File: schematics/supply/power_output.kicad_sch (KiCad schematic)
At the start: 41 parts, among them Q10 IRLML0030, U2 EL817, U23 TL331, U24 INA169, U9 IRS2153S

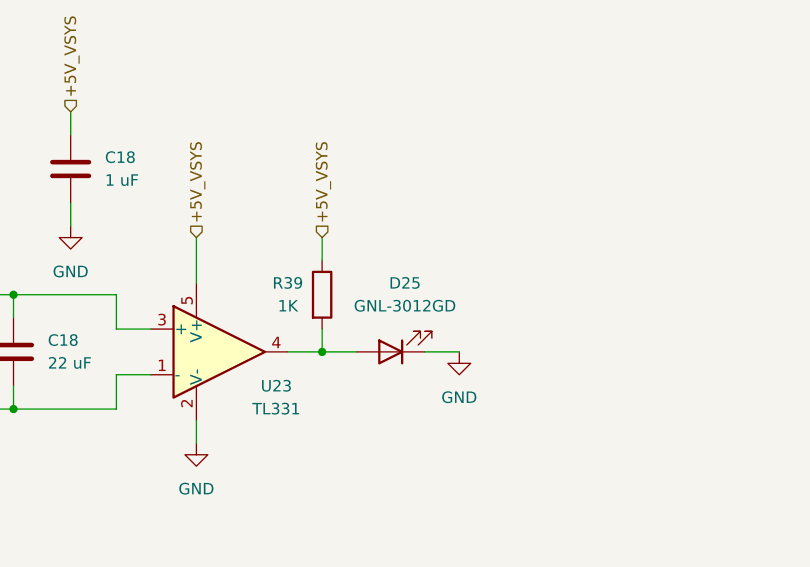
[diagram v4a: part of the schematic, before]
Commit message: Fixed problem with 20V on one leg of comparator
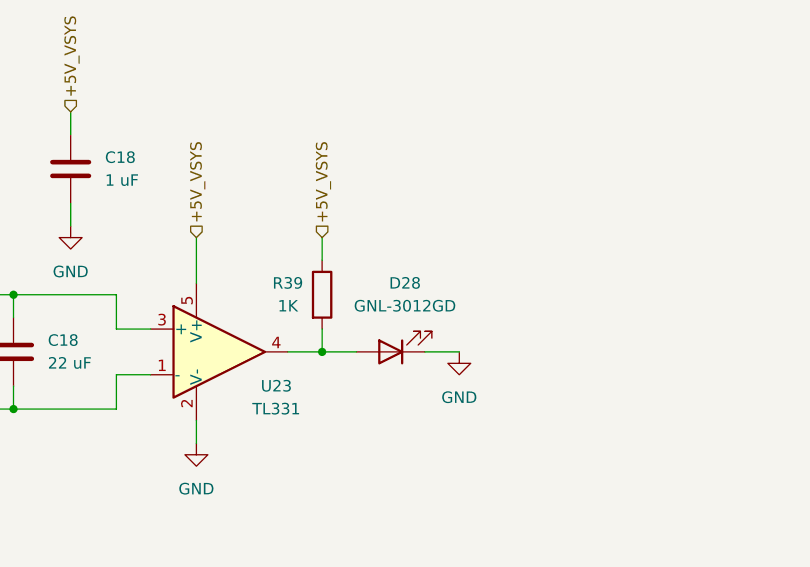
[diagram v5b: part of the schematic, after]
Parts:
- renumbered D25 to D28

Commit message: Board prepared to order
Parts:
- L2: value SPM6550T-2R2M -> SPM6550T-R68M
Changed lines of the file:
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@@
       (effects (font (size 1.27 1.27)))
     )
-    (property "Value" "SPM6550T-2R2M" (at 269.24 132.08 90)
+    (property "Value" "SPM6550T-R68M" (at 269.24 132.08 90)
       (effects (font (size 1.27 1.27)))
     )

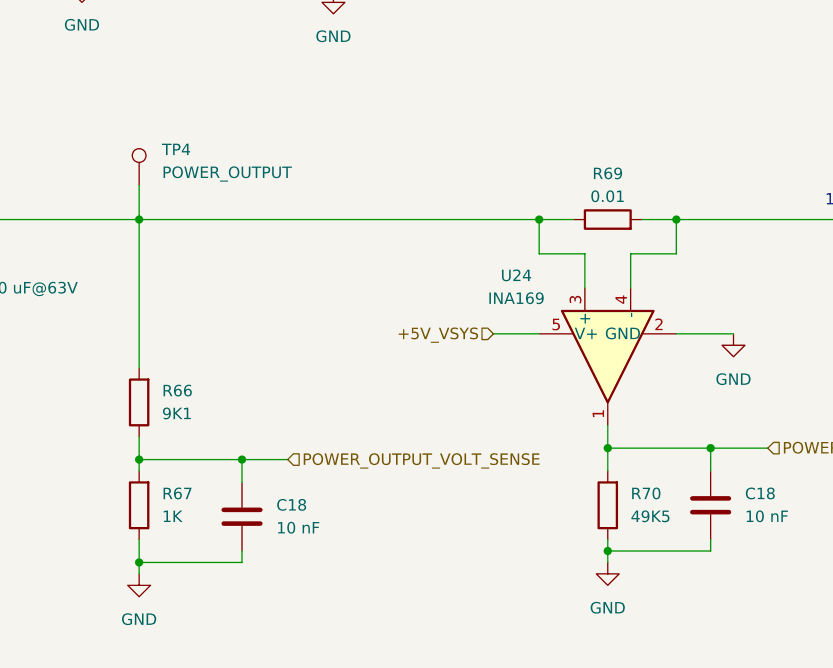
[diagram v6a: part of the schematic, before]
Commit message: One board settings changed from 4-layers to 2-layers to reduce it's price
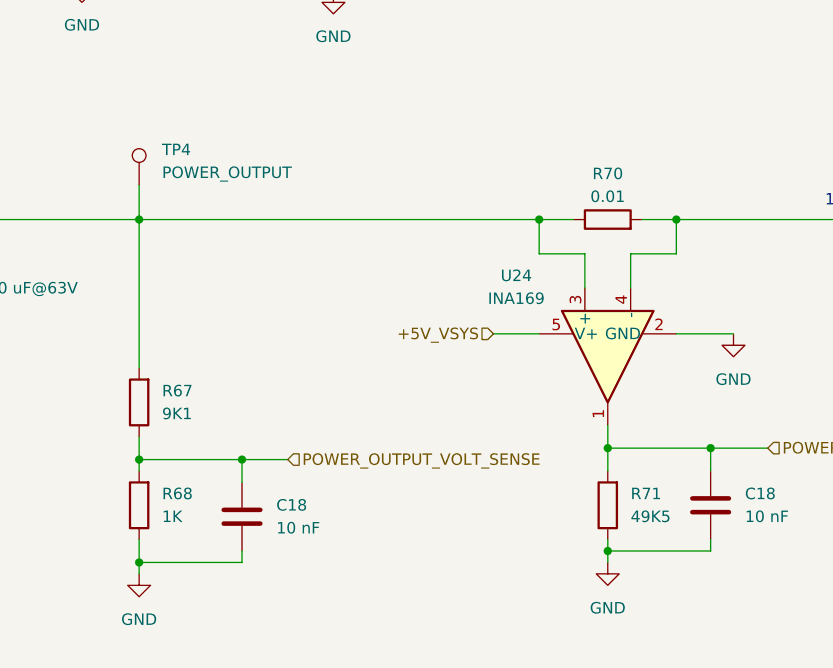
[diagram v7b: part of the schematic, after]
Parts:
- renumbered R66 to R67, R67 to R68, R69 to R70, R70 to R71
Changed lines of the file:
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@@
         )
         (path "/1e139717-fcd1-4008-a6ea-4c993845e928/4671650e-ec71-47e3-a051-fc2ad6d25f63"
-          (reference "R62") (unit 1)
+          (reference "R63") (unit 1)
         )
       )
@@
         )
         (path "/1e139717-fcd1-4008-a6ea-4c993845e928/4671650e-ec71-47e3-a051-fc2ad6d25f63"
-          (reference "R60") (unit 1)
+          (reference "R61") (unit 1)
         )
       )
@@
         )
         (path "/1e139717-fcd1-4008-a6ea-4c993845e928/4671650e-ec71-47e3-a051-fc2ad6d25f63"
-          (reference "R68") (unit 1)
+          (reference "R69") (unit 1)
         )
       )
@@
         )
         (path "/1e139717-fcd1-4008-a6ea-4c993845e928/4671650e-ec71-47e3-a051-fc2ad6d25f63"
-          (reference "R59") (unit 1)
+          (reference "R60") (unit 1)
         )
       )
@@
         )
         (path "/1e139717-fcd1-4008-a6ea-4c993845e928/4671650e-ec71-47e3-a051-fc2ad6d25f63"
-          (reference "R63") (unit 1)
+          (reference "R64") (unit 1)
         )
       )
@@
   (symbol (lib_id "Device:R") (at 358.14 167.64 180) (unit 1)
     (in_bom yes) (on_board yes) (dnp no) (fields_autoplaced)
-    (property "Reference" "R70" (at 360.68 166.37 0)
+    (property "Reference" "R71" (at 360.68 166.37 0)
       (effects (font (size 1.27 1.27)) (justify right))
     )
@@
       (project "supply"
         (path "/1e139717-fcd1-4008-a6ea-4c993845e928/4671650e-ec71-47e3-a051-fc2ad6d25f63"
-          (reference "R70") (unit 1)
+          (reference "R71") (unit 1)
         )
       )
@@
         )
         (path "/1e139717-fcd1-4008-a6ea-4c993845e928/4671650e-ec71-47e3-a051-fc2ad6d25f63"
-          (reference "R64") (unit 1)
+          (reference "R65") (unit 1)
         )
       )
@@
         )
         (path "/1e139717-fcd1-4008-a6ea-4c993845e928/4671650e-ec71-47e3-a051-fc2ad6d25f63"
-          (reference "R65") (unit 1)
+          (reference "R66") (unit 1)
         )
       )
@@
   (symbol (lib_id "Device:R") (at 306.07 167.64 180) (unit 1)
     (in_bom yes) (on_board yes) (dnp no) (fields_autoplaced)
-    (property "Reference" "R67" (at 308.61 166.37 0)
+    (property "Reference" "R68" (at 308.61 166.37 0)
       (effects (font (size 1.27 1.27)) (justify right))
     )
@@
       (project "supply"
         (path "/1e139717-fcd1-4008-a6ea-4c993845e928/4671650e-ec71-47e3-a051-fc2ad6d25f63"
-          (reference "R67") (unit 1)
+          (reference "R68") (unit 1)
         )
       )
@@
         )
         (path "/1e139717-fcd1-4008-a6ea-4c993845e928/4671650e-ec71-47e3-a051-fc2ad6d25f63"
-          (reference "R61") (unit 1)
+          (reference "R62") (unit 1)
         )
       )
@@
   (symbol (lib_id "Device:R") (at 306.07 156.21 180) (unit 1)
     (in_bom yes) (on_board yes) (dnp no) (fields_autoplaced)
-    (property "Reference" "R66" (at 308.61 154.94 0)
+    (property "Reference" "R67" (at 308.61 154.94 0)
       (effects (font (size 1.27 1.27)) (justify right))
     )
@@
       (project "supply"
         (path "/1e139717-fcd1-4008-a6ea-4c993845e928/4671650e-ec71-47e3-a051-fc2ad6d25f63"
-          (reference "R66") (unit 1)
+          (reference "R67") (unit 1)
         )
       )
@@
   (symbol (lib_id "Device:R") (at 358.14 135.89 90) (unit 1)
     (in_bom yes) (on_board yes) (dnp no) (fields_autoplaced)
-    (property "Reference" "R69" (at 358.14 130.81 90)
+    (property "Reference" "R70" (at 358.14 130.81 90)
       (effects (font (size 1.27 1.27)))
     )
@@
       (project "supply"
         (path "/1e139717-fcd1-4008-a6ea-4c993845e928/4671650e-ec71-47e3-a051-fc2ad6d25f63"
-          (reference "R69") (unit 1)
-        )
-      )
+          (reference "R70") (unit 1)
+        )
+      )
